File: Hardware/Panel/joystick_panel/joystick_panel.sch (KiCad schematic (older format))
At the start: 13 parts

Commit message: Panel design
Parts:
- added H10, H12, H13, H9: Mounting_Hole, MountingHole:MountingHole_2.5mm_Pad, symbol Kosmo:Mounting_Hole
- gave numbers to parts that had none: 4
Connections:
- net GND: now also H10.1, H12.1, H13.1, H9.1
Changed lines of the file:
@@
 $EndComp
 $Comp
-L Kosmo:Pot_Hole H?
+L Kosmo:Pot_Hole H5
 U 1 1 6158F273
 P 4000 2000
-F 0 "H?" H 4185 1992 50  0000 L CNN
+F 0 "H5" H 4185 1992 50  0000 L CNN
 F 1 "Pot_Hole" H 4185 1901 50  0000 L CNN
 F 2 "Kosmo_panel:Kosmo_Pot_Hole" H 4000 2000 50  0001 C CNN
@@
 $EndComp
 $Comp
-L power:GND #PWR?
+L power:GND #PWR05
 U 1 1 6158F279
 P 4000 2250
-F 0 "#PWR?" H 4000 2000 50  0001 C CNN
+F 0 "#PWR05" H 4000 2000 50  0001 C CNN
 F 1 "GND" H 4005 2077 50  0000 C CNN
 F 2 "" H 4000 2250 50  0001 C CNN
@@
 $EndComp
 $Comp
-L Kosmo:Pot_Hole H?
+L Kosmo:Pot_Hole H7
 U 1 1 6158F8ED
 P 5000 2000
-F 0 "H?" H 5185 1992 50  0000 L CNN
+F 0 "H7" H 5185 1992 50  0000 L CNN
 F 1 "Pot_Hole" H 5185 1901 50  0000 L CNN
 F 2 "Kosmo_panel:Kosmo_Pot_Hole" H 5000 2000 50  0001 C CNN
@@
 $EndComp
 $Comp
-L power:GND #PWR?
+L power:GND #PWR07
 U 1 1 6158F8F3
 P 5000 2250
-F 0 "#PWR?" H 5000 2000 50  0001 C CNN
+F 0 "#PWR07" H 5000 2000 50  0001 C CNN
 F 1 "GND" H 5005 2077 50  0000 C CNN
 F 2 "" H 5000 2250 50  0001 C CNN
@@
 $EndComp
 $Comp
-L Kosmo:Pot_Hole H?
+L Kosmo:Pot_Hole H6
 U 1 1 6158FE67
 P 4000 3000
-F 0 "H?" H 4185 2992 50  0000 L CNN
+F 0 "H6" H 4185 2992 50  0000 L CNN
 F 1 "Pot_Hole" H 4185 2901 50  0000 L CNN
 F 2 "Kosmo_panel:Kosmo_Pot_Hole" H 4000 3000 50  0001 C CNN
@@
 $EndComp
 $Comp
-L power:GND #PWR?
+L power:GND #PWR06
 U 1 1 6158FE6D
 P 4000 3250
-F 0 "#PWR?" H 4000 3000 50  0001 C CNN
+F 0 "#PWR06" H 4000 3000 50  0001 C CNN
 F 1 "GND" H 4005 3077 50  0000 C CNN
 F 2 "" H 4000 3250 50  0001 C CNN
@@
 $EndComp
 $Comp
-L Kosmo:Pot_Hole H?
+L Kosmo:Pot_Hole H8
 U 1 1 61590587
 P 5000 3000
-F 0 "H?" H 5185 2992 50  0000 L CNN
+F 0 "H8" H 5185 2992 50  0000 L CNN
 F 1 "Pot_Hole" H 5185 2901 50  0000 L CNN
 F 2 "Kosmo_panel:Kosmo_Pot_Hole" H 5000 3000 50  0001 C CNN
@@
 $EndComp
 $Comp
-L power:GND #PWR?
+L power:GND #PWR08
 U 1 1 6159058D
 P 5000 3250
-F 0 "#PWR?" H 5000 3000 50  0001 C CNN
+F 0 "#PWR08" H 5000 3000 50  0001 C CNN
 F 1 "GND" H 5005 3077 50  0000 C CNN
 F 2 "" H 5000 3250 50  0001 C CNN
@@
 	1    0    0    -1
 $EndComp
+$Comp
+L Kosmo:Mounting_Hole H9
+U 1 1 615921BF
+P 6450 3350
+F 0 "H9" H 6550 3399 50  0000 L CNN
+F 1 "Mounting_Hole" H 6550 3308 50  0000 L CNN
+F 2 "MountingHole:MountingHole_2.5mm_Pad" H 6450 3350 50  0001 C CNN
+F 3 "" H 6450 3350 50  0001 C CNN
+	1    6450 3350
+	1    0    0    -1
+$EndComp
+$Comp
+L power:GND #PWR09
+U 1 1 615923D5
+P 6450 3450
+F 0 "#PWR09" H 6450 3200 50  0001 C CNN
+F 1 "GND" H 6455 3277 50  0000 C CNN
+F 2 "" H 6450 3450 50  0001 C CNN
+F 3 "" H 6450 3450 50  0001 C CNN
+	1    6450 3450
+	1    0    0    -1
+$EndComp
+$Comp
+L Kosmo:Mounting_Hole H12
+U 1 1 61592D79
+P 7150 3350
+F 0 "H12" H 7250 3399 50  0000 L CNN
+F 1 "Mounting_Hole" H 7250 3308 50  0000 L CNN
+F 2 "MountingHole:MountingHole_2.5mm_Pad" H 7150 3350 50  0001 C CNN
+F 3 "" H 7150 3350 50  0001 C CNN
+	1    7150 3350
+	1    0    0    -1
+$EndComp
+$Comp
+L power:GND #PWR013
+U 1 1 61592D7F
+P 7150 3450
+F 0 "#PWR013" H 7150 3200 50  0001 C CNN
+F 1 "GND" H 7155 3277 50  0000 C CNN
+F 2 "" H 7150 3450 50  0001 C CNN
+F 3 "" H 7150 3450 50  0001 C CNN
+	1    7150 3450
+	1    0    0    -1
+$EndComp
+$Comp
+L Kosmo:Mounting_Hole H10
+U 1 1 6159343F
+P 6450 3800
+F 0 "H10" H 6550 3849 50  0000 L CNN
+F 1 "Mounting_Hole" H 6550 3758 50  0000 L CNN
+F 2 "MountingHole:MountingHole_2.5mm_Pad" H 6450 3800 50  0001 C CNN
+F 3 "" H 6450 3800 50  0001 C CNN
+	1    6450 3800
+	1    0    0    -1
+$EndComp
+$Comp
+L power:GND #PWR010
+U 1 1 61593445
+P 6450 3900
+F 0 "#PWR010" H 6450 3650 50  0001 C CNN
+F 1 "GND" H 6455 3727 50  0000 C CNN
+F 2 "" H 6450 3900 50  0001 C CNN
+F 3 "" H 6450 3900 50  0001 C CNN
+	1    6450 3900
+	1    0    0    -1
+$EndComp
+$Comp
+L Kosmo:Mounting_Hole H13
+U 1 1 6159393B
+P 7150 3800
+F 0 "H13" H 7250 3849 50  0000 L CNN
+F 1 "Mounting_Hole" H 7250 3758 50  0000 L CNN
+F 2 "MountingHole:MountingHole_2.5mm_Pad" H 7150 3800 50  0001 C CNN
+F 3 "" H 7150 3800 50  0001 C CNN
+	1    7150 3800
+	1    0    0    -1
+$EndComp
+$Comp
+L power:GND #PWR014
+U 1 1 61593941
+P 7150 3900
+F 0 "#PWR014" H 7150 3650 50  0001 C CNN
+F 1 "GND" H 7155 3727 50  0000 C CNN
+F 2 "" H 7150 3900 50  0001 C CNN
+F 3 "" H 7150 3900 50  0001 C CNN
+	1    7150 3900
+	1    0    0    -1
+$EndComp

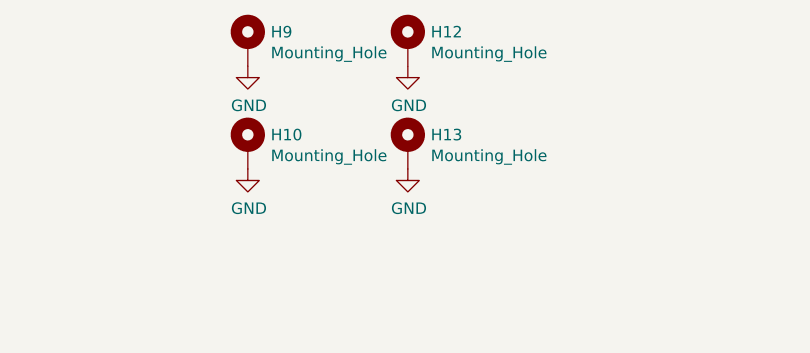
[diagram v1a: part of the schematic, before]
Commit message: Belated .gitignore; switch to panel mounted pots implying board and panel changes
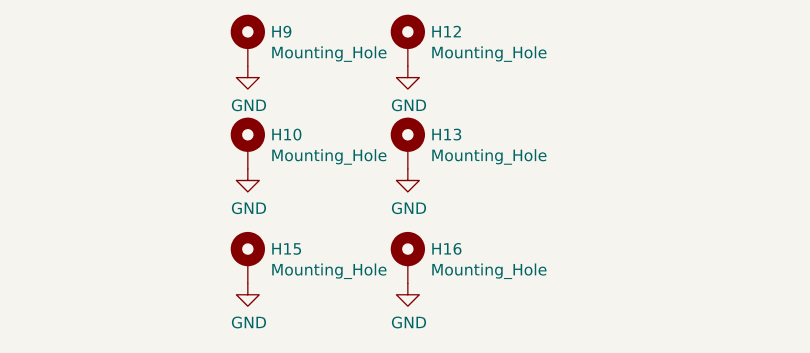
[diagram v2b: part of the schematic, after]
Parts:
- added H15, H16: Mounting_Hole, ao_tht:MountingHole_3.2mm_M3, symbol Kosmo:Mounting_Hole
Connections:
- net GND: now also H15.1, H16.1
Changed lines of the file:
@@
 $EndComp
 $Comp
-L Kosmo:Mounting_Hole H10
-U 1 1 6159343F
-P 6450 3800
-F 0 "H10" H 6550 3849 50  0000 L CNN
-F 1 "Mounting_Hole" H 6550 3758 50  0000 L CNN
-F 2 "MountingHole:MountingHole_2.5mm_Pad" H 6450 3800 50  0001 C CNN
-F 3 "" H 6450 3800 50  0001 C CNN
-	1    6450 3800
+L power:GND #PWR014
+U 1 1 61593941
+P 7150 3900
+F 0 "#PWR014" H 7150 3650 50  0001 C CNN
+F 1 "GND" H 7155 3727 50  0000 C CNN
+F 2 "" H 7150 3900 50  0001 C CNN
+F 3 "" H 7150 3900 50  0001 C CNN
+	1    7150 3900
+	1    0    0    -1
+$EndComp
+$Comp
+L Kosmo:Mounting_Hole H13
+U 1 1 6159393B
+P 7150 3800
+F 0 "H13" H 7250 3849 50  0000 L CNN
+F 1 "Mounting_Hole" H 7250 3758 50  0000 L CNN
+F 2 "MountingHole:MountingHole_2.5mm_Pad" H 7150 3800 50  0001 C CNN
+F 3 "" H 7150 3800 50  0001 C CNN
+	1    7150 3800
 	1    0    0    -1
 $EndComp
@@
 $EndComp
 $Comp
-L Kosmo:Mounting_Hole H13
-U 1 1 6159393B
-P 7150 3800
-F 0 "H13" H 7250 3849 50  0000 L CNN
-F 1 "Mounting_Hole" H 7250 3758 50  0000 L CNN
-F 2 "MountingHole:MountingHole_2.5mm_Pad" H 7150 3800 50  0001 C CNN
-F 3 "" H 7150 3800 50  0001 C CNN
-	1    7150 3800
+L Kosmo:Mounting_Hole H10
+U 1 1 6159343F
+P 6450 3800
+F 0 "H10" H 6550 3849 50  0000 L CNN
+F 1 "Mounting_Hole" H 6550 3758 50  0000 L CNN
+F 2 "MountingHole:MountingHole_2.5mm_Pad" H 6450 3800 50  0001 C CNN
+F 3 "" H 6450 3800 50  0001 C CNN
+	1    6450 3800
 	1    0    0    -1
 $EndComp
 $Comp
-L power:GND #PWR014
-U 1 1 61593941
-P 7150 3900
-F 0 "#PWR014" H 7150 3650 50  0001 C CNN
-F 1 "GND" H 7155 3727 50  0000 C CNN
-F 2 "" H 7150 3900 50  0001 C CNN
-F 3 "" H 7150 3900 50  0001 C CNN
-	1    7150 3900
+L power:GND #PWR016
+U 1 1 6179E13C
+P 7150 4400
+F 0 "#PWR016" H 7150 4150 50  0001 C CNN
+F 1 "GND" H 7155 4227 50  0000 C CNN
+F 2 "" H 7150 4400 50  0001 C CNN
+F 3 "" H 7150 4400 50  0001 C CNN
+	1    7150 4400
 	1    0    0    -1
 $EndComp
+$Comp
+L Kosmo:Mounting_Hole H16
+U 1 1 6179E142
+P 7150 4300
+F 0 "H16" H 7250 4349 50  0000 L CNN
+F 1 "Mounting_Hole" H 7250 4258 50  0000 L CNN
+F 2 "ao_tht:MountingHole_3.2mm_M3" H 7150 4300 50  0001 C CNN
+F 3 "" H 7150 4300 50  0001 C CNN
+	1    7150 4300
+	1    0    0    -1
+$EndComp
+$Comp
+L power:GND #PWR015
+U 1 1 6179E148
+P 6450 4400
+F 0 "#PWR015" H 6450 4150 50  0001 C CNN
+F 1 "GND" H 6455 4227 50  0000 C CNN
+F 2 "" H 6450 4400 50  0001 C CNN
+F 3 "" H 6450 4400 50  0001 C CNN
+	1    6450 4400
+	1    0    0    -1
+$EndComp
+$Comp
+L Kosmo:Mounting_Hole H15
+U 1 1 6179E14E
+P 6450 4300
+F 0 "H15" H 6550 4349 50  0000 L CNN
+F 1 "Mounting_Hole" H 6550 4258 50  0000 L CNN
+F 2 "ao_tht:MountingHole_3.2mm_M3" H 6450 4300 50  0001 C CNN
+F 3 "" H 6450 4300 50  0001 C CNN
+	1    6450 4300
+	1    0    0    -1
+$EndComp

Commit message: Add gain trimmers and test points
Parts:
- added H17, H18, H19, H20: Trimmer_Hole, Kosmo_panel:Kosmo_Trimmer_Pot_Hole, symbol Kosmo:Trimmer_Hole
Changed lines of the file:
@@
+	1    0    0    -1
+$EndComp
+$Comp
+L Kosmo:Trimmer_Hole H17
+U 1 1 618B403B
+P 5100 4300
+F 0 "H17" H 5170 4346 50  0000 L CNN
+F 1 "Trimmer_Hole" H 5170 4255 50  0000 L CNN
+F 2 "Kosmo_panel:Kosmo_Trimmer_Pot_Hole" H 5010 4420 50  0001 C CNN
+F 3 "" H 5100 4300 50  0001 C CNN
+	1    5100 4300
+	1    0    0    -1
+$EndComp
+$Comp
+L Kosmo:Trimmer_Hole H18
+U 1 1 618B4477
+P 5100 4500
+F 0 "H18" H 5170 4546 50  0000 L CNN
+F 1 "Trimmer_Hole" H 5170 4455 50  0000 L CNN
+F 2 "Kosmo_panel:Kosmo_Trimmer_Pot_Hole" H 5010 4620 50  0001 C CNN
+F 3 "" H 5100 4500 50  0001 C CNN
+	1    5100 4500
+	1    0    0    -1
+$EndComp
+$Comp
+L Kosmo:Trimmer_Hole H19
+U 1 1 618B50EC
+P 5100 4700
+F 0 "H19" H 5170 4746 50  0000 L CNN
+F 1 "Trimmer_Hole" H 5170 4655 50  0000 L CNN
+F 2 "Kosmo_panel:Kosmo_Trimmer_Pot_Hole" H 5010 4820 50  0001 C CNN
+F 3 "" H 5100 4700 50  0001 C CNN
+	1    5100 4700
+	1    0    0    -1
+$EndComp
+$Comp
+L Kosmo:Trimmer_Hole H20
+U 1 1 618B50F2
+P 5100 4900
+F 0 "H20" H 5170 4946 50  0000 L CNN
+F 1 "Trimmer_Hole" H 5170 4855 50  0000 L CNN
+F 2 "Kosmo_panel:Kosmo_Trimmer_Pot_Hole" H 5010 5020 50  0001 C CNN
+F 3 "" H 5100 4900 50  0001 C CNN
+	1    5100 4900
 	1    0    0    -1
 $EndComp

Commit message: Move trimmers and TPs to back
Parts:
- removed H17, H18, H19, H20: Trimmer_Hole, Kosmo_panel:Kosmo_Trimmer_Pot_Hole, symbol Kosmo:Trimmer_Hole
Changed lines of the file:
@@
-	1    0    0    -1
-$EndComp
-$Comp
-L Kosmo:Trimmer_Hole H17
-U 1 1 618B403B
-P 5100 4300
-F 0 "H17" H 5170 4346 50  0000 L CNN
-F 1 "Trimmer_Hole" H 5170 4255 50  0000 L CNN
-F 2 "Kosmo_panel:Kosmo_Trimmer_Pot_Hole" H 5010 4420 50  0001 C CNN
-F 3 "" H 5100 4300 50  0001 C CNN
-	1    5100 4300
-	1    0    0    -1
-$EndComp
-$Comp
-L Kosmo:Trimmer_Hole H18
-U 1 1 618B4477
-P 5100 4500
-F 0 "H18" H 5170 4546 50  0000 L CNN
-F 1 "Trimmer_Hole" H 5170 4455 50  0000 L CNN
-F 2 "Kosmo_panel:Kosmo_Trimmer_Pot_Hole" H 5010 4620 50  0001 C CNN
-F 3 "" H 5100 4500 50  0001 C CNN
-	1    5100 4500
-	1    0    0    -1
-$EndComp
-$Comp
-L Kosmo:Trimmer_Hole H19
-U 1 1 618B50EC
-P 5100 4700
-F 0 "H19" H 5170 4746 50  0000 L CNN
-F 1 "Trimmer_Hole" H 5170 4655 50  0000 L CNN
-F 2 "Kosmo_panel:Kosmo_Trimmer_Pot_Hole" H 5010 4820 50  0001 C CNN
-F 3 "" H 5100 4700 50  0001 C CNN
-	1    5100 4700
-	1    0    0    -1
-$EndComp
-$Comp
-L Kosmo:Trimmer_Hole H20
-U 1 1 618B50F2
-P 5100 4900
-F 0 "H20" H 5170 4946 50  0000 L CNN
-F 1 "Trimmer_Hole" H 5170 4855 50  0000 L CNN
-F 2 "Kosmo_panel:Kosmo_Trimmer_Pot_Hole" H 5010 5020 50  0001 C CNN
-F 3 "" H 5100 4900 50  0001 C CNN
-	1    5100 4900
 	1    0    0    -1
 $EndComp
